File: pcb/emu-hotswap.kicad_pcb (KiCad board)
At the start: 2 copper layers, 159.1 x 114.4 mm, 74 parts, among them J1 TRRS, SW1 SW_Push, SW10 SW_Push, SW11 SW_Push, SW12 SW_Push, SW13 SW_Push, SW14 SW_Push, SW15 SW_Push, SW16 SW_Push, SW17 SW_Push, SW18 SW_Push, SW19 SW_Push, SW2 SW_Push, SW20 SW_Push, SW21 SW_Push, SW22 SW_Push, SW23 SW_Push, SW24 SW_Push, SW25 SW_Push, SW26 SW_Push, SW27 SW_Push, SW28 SW_Push, SW29 SW_Push, SW3 SW_Push, SW30 SW_Push, SW31 SW_Push, SW4 SW_Push, SW5 SW_Push, SW6 SW_Push, SW7 SW_Push, SW8 SW_Push, SW9 SW_Push, U1 ProMicro

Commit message: Work in progress
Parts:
- removed the D10 at (149.8, 127.3)
- added D10: 1N4148, used_footprints:Diode_Hybrid_SOD-123, F.Cu at (221.6, 96.2)
- added D10: 1N4148, used_footprints:Diode_Hybrid_SOD-123, F.Cu at (153.9, 131.1)
- added SW10: SW_Push, used_footprints:Switch_Mx_Hotswap_1u, F.Cu at (223.3, 91.0)
- SW10, SW15: footprint used_footprints:Switch_Mx_Hotswap_1u -> used_footprints:Switch_Mx_Hotswap_1.25u
- U1: footprint used_footprints:ProMicro_Dual -> used_footprints:Pro_Micro
- moved HM3 100.2 mm to (214.6, 75.1)
- moved HM2 59.9 mm to (134.3, 73.0)
- moved U1 26.5 mm to (112.3, 70.0), turned to 90 degrees
- moved SW30 17.5 mm to (222.7, 113.0), turned to 153 degrees
- moved D30 17.3 mm to (220.2, 117.9), turned to 153 degrees
- moved R1 11.3 mm to (225.1, 67.1)
- moved R2 11.3 mm to (222.2, 67.1)
- moved HM1 10.4 mm to (216.7, 124.0)
- moved J1 9.97 mm to (231.0, 62.3)
- moved JP1 9.97 mm to (228.9, 77.2)
- moved JP2 9.97 mm to (228.9, 77.2)
- moved JP3 9.97 mm to (233.1, 77.2)
- moved JP4 9.97 mm to (233.1, 77.2)
- moved SW25 8.29 mm to (222.7, 137.1), turned to 144 degrees
- moved D25 7.62 mm to (219.4, 141.5), turned to 144 degrees
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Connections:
- U1 pad 13: /LED -> (no net)
- U1 pad 14: Net-(U1-Pad14) -> (no net)
- U1 pad 15: Net-(U1-Pad15) -> (no net)
- U1 pad 16: Net-(U1-Pad16) -> (no net)
- U1 pad 17: Net-(U1-Pad17) -> (no net)
- U1 pad 24: Net-(U1-Pad24) -> (no net)
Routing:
- net /col4: track 367.6 -> 0.00 mm, vias 2 -> 0
- net /col5: track 361.5 -> 0.00 mm, vias 3 -> 0
- net /col3: track 341.1 -> 0.00 mm, vias 2 -> 0
- net /col2: track 301.2 -> 0.00 mm, vias 3 -> 0
- net /rowA: track 289.0 -> 0.00 mm, vias 2 -> 0
- net /rowE: track 282.7 -> 0.00 mm, vias 2 -> 0
- net /col1: track 264.9 -> 0.00 mm, vias 2 -> 0
- net GND: track 223.2 -> 0.00 mm, vias 2 -> 0
- net /rowD: track 220.0 -> 0.00 mm, vias 5 -> 0
- net /rowC: track 206.7 -> 0.00 mm, vias 7 -> 0
- net VCC: track 202.4 -> 0.00 mm, vias 1 -> 0
- net /col0: track 194.7 -> 0.00 mm, vias 2 -> 0
- net SCL: track 194.0 -> 0.00 mm, vias 2 -> 0
- net SDA: track 189.8 -> 0.00 mm, vias 8 -> 0
- net /RST: track 187.9 -> 0.00 mm, vias 1 -> 0
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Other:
- board size 159.1 x 114.4 mm -> 160.3 x 119.3 mm
- board text removed: "14.5 degrees"

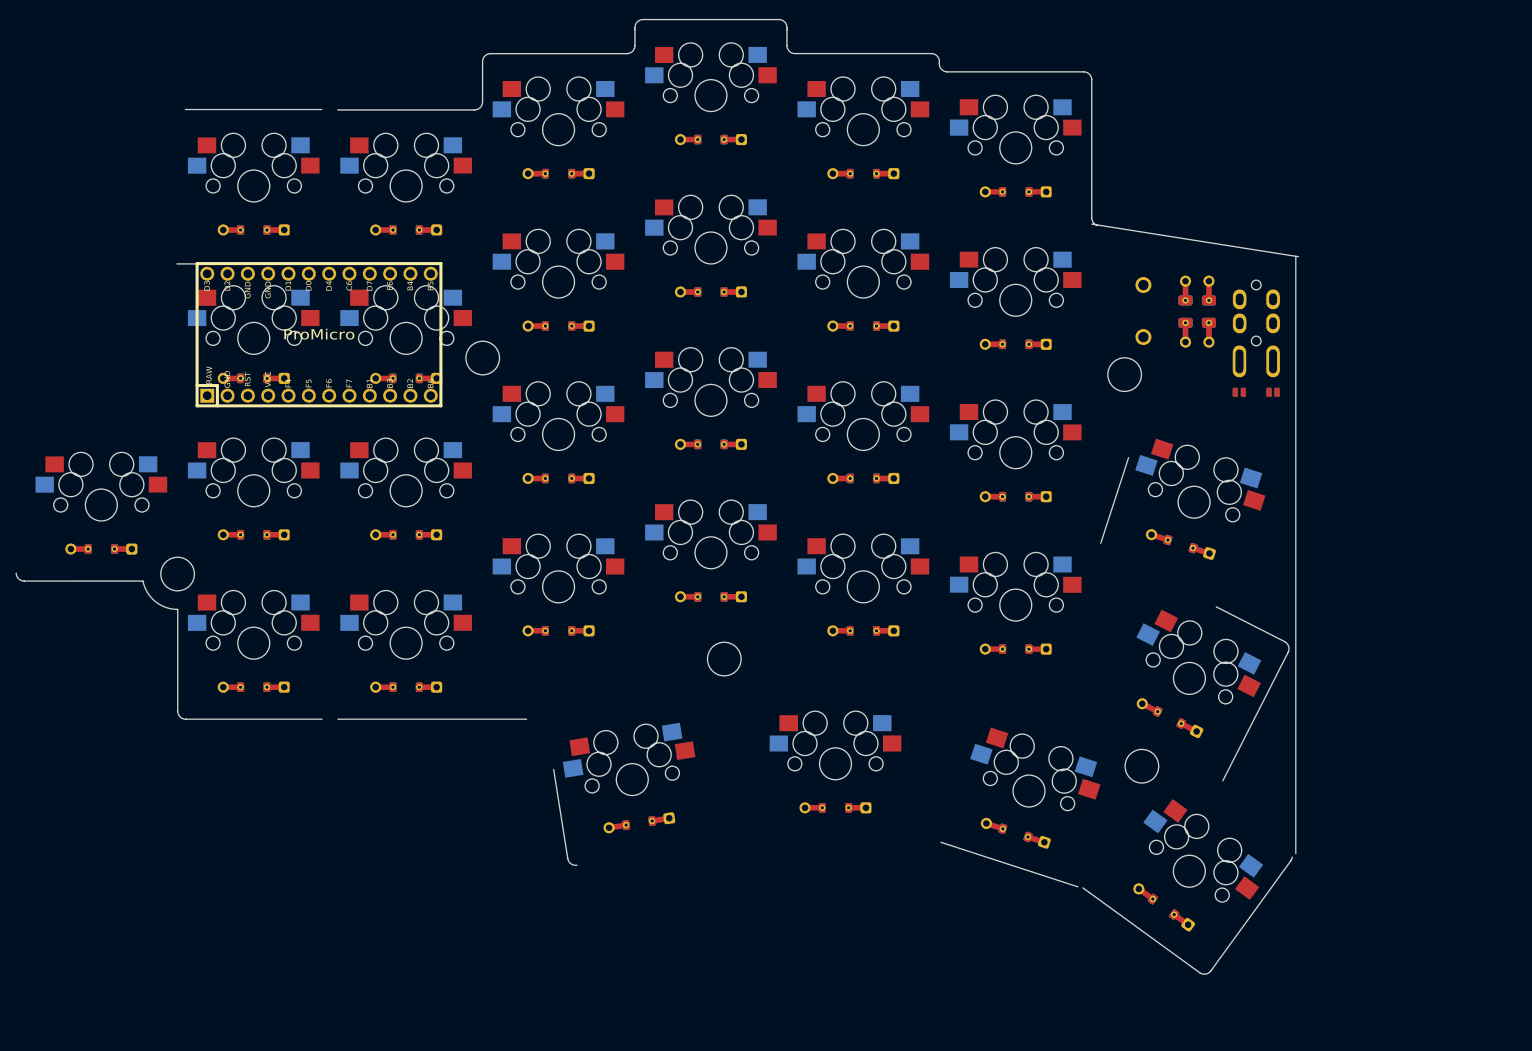
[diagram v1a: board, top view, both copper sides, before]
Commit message: Added new footprints
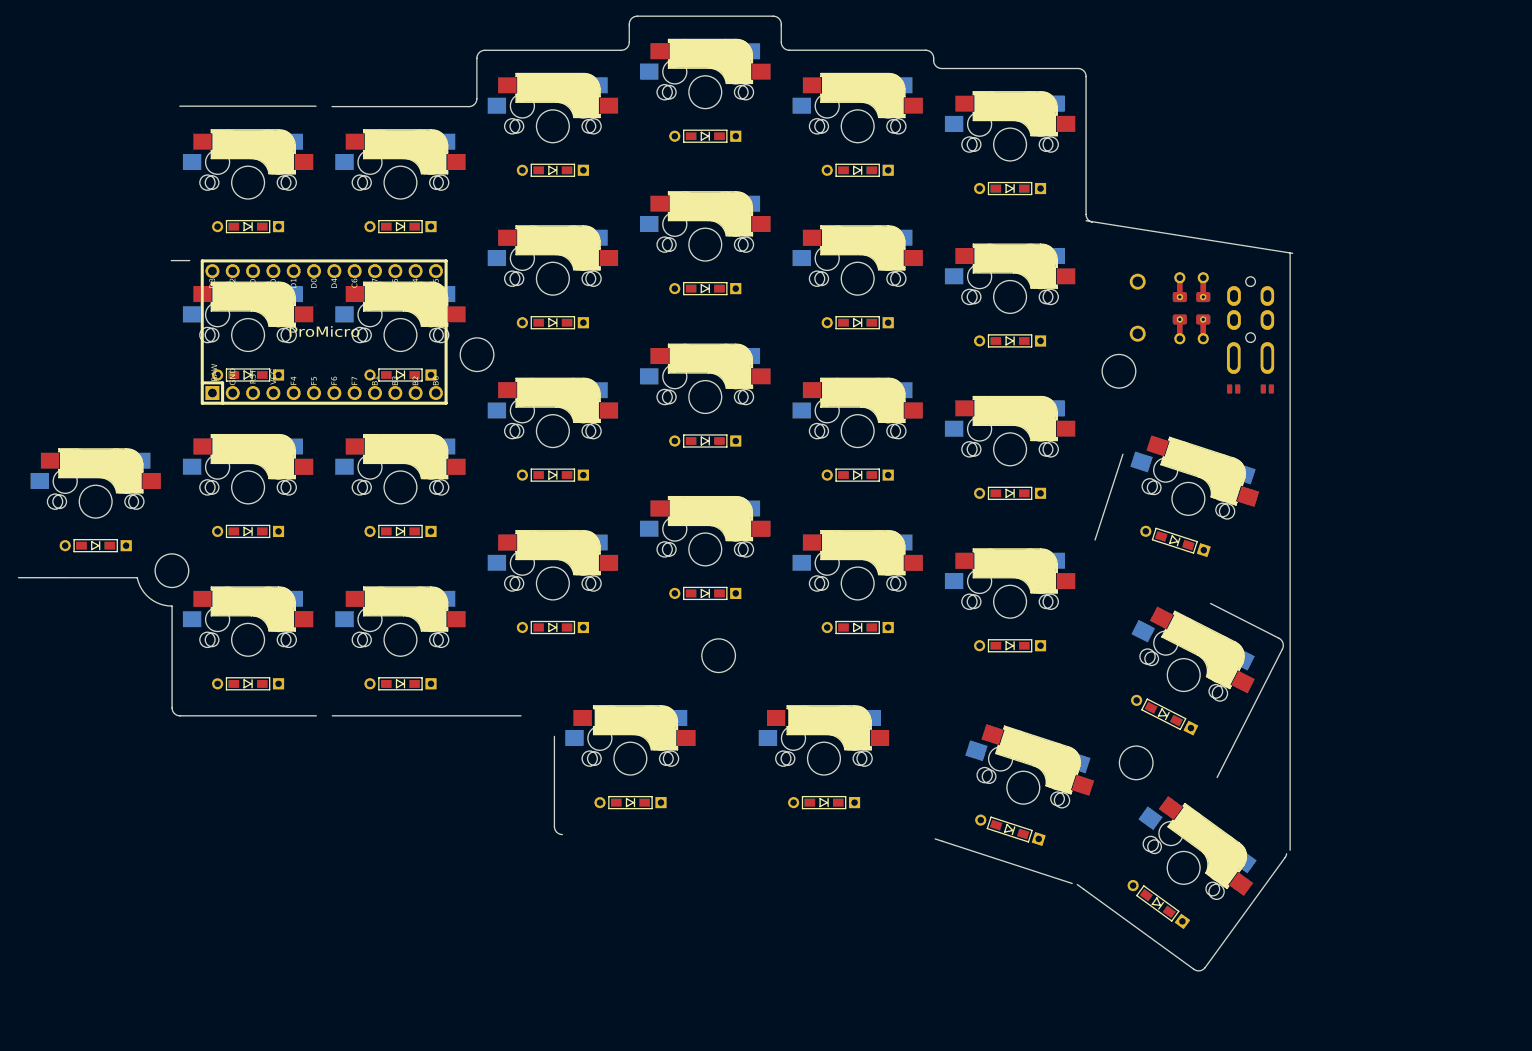
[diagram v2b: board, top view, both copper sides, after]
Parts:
- D1, D10 (x2), D11, D12, D13, D14, D15, D16, D17, D18, D19, D2, D20, D21, D22, D23, D24, D25, D26, D27, D28, D29, D3, D30, D4, D5, D6, D7, D8, D9: footprint used_footprints:Diode_Hybrid_SOD-123 -> used_footprints:D3_TH_SMD
- SW1, SW10, SW11, SW12, SW13, SW14, SW16, SW17, SW18, SW19, SW2, SW20, SW21, SW22, SW23, SW24, SW25, SW26, SW27, SW28, SW29, SW3, SW30, SW4, SW5, SW6, SW7, SW8, SW9: footprint used_footprints:Switch_Mx_Hotswap_1u -> used_footprints:CherryMX_MidHeight_Hotswap_1u
- SW10, SW15: footprint used_footprints:Switch_Mx_Hotswap_1.25u -> used_footprints:CherryMX_MidHeight_Hotswap_1.25u
- moved D10 2.77 mm to (152.8, 128.5), turned to 180 degrees
- moved SW10 2.63 mm to (152.8, 123.0), turned to 180 degrees
- moved D15 1.57 mm to (177.0, 128.5)
- moved SW15 1.57 mm to (177.0, 123.0)
- moved D10 0.82 mm to (220.8, 95.8)
- moved D11 0.82 mm to (143.1, 49.5)
- moved D12 0.82 mm to (143.1, 68.5)
- moved D13 0.82 mm to (143.1, 87.6)
- moved D14 0.82 mm to (143.1, 106.6)
- moved D17 0.82 mm to (162.2, 64.2)
- moved D18 0.82 mm to (162.2, 83.3)
- moved D19 0.82 mm to (162.2, 102.3)
- moved D21 0.82 mm to (181.2, 49.5)
- moved D22 0.82 mm to (181.2, 68.5)
- moved D23 0.82 mm to (181.2, 87.6)
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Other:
- board size 160.3 x 119.3 mm -> 159.3 x 119.3 mm

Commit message: Lined everything up to grid 0.05mm
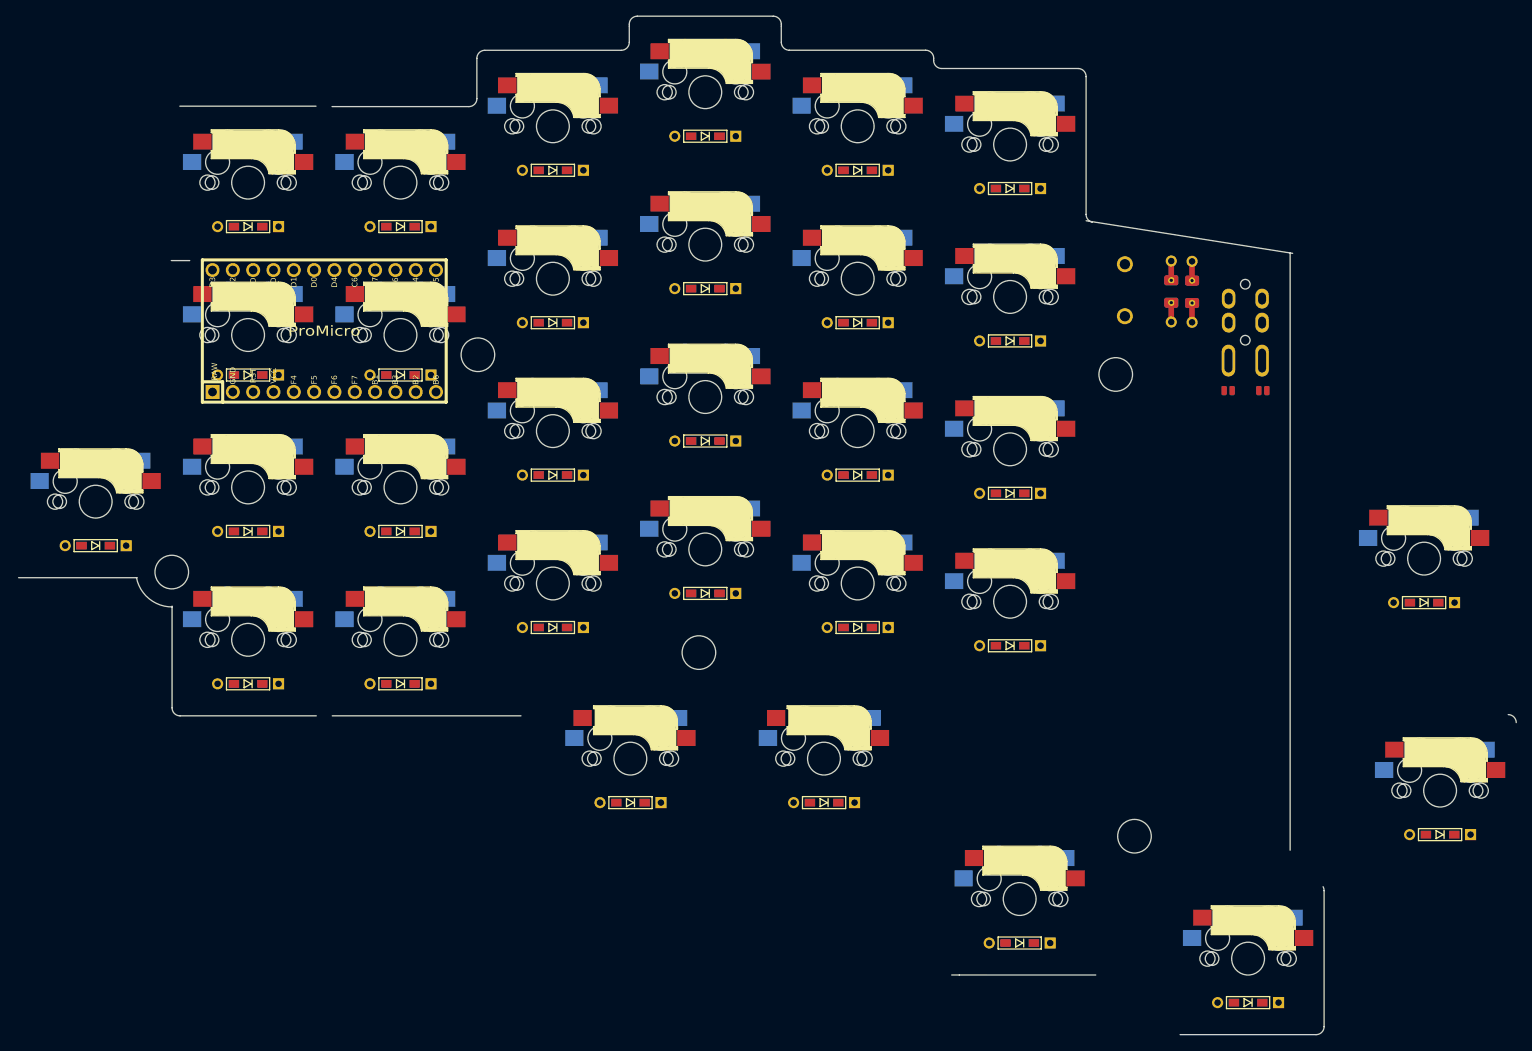
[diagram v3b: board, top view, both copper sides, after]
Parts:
- added G***: LOGO, used_footprints:emu-logo, F.Cu at (55.8, 53.5)
- moved D30 37.7 mm to (254.0, 132.5), turned to 180 degrees
- moved SW30 35.1 mm to (254.0, 127.0), turned to 180 degrees
- moved D10 32.1 mm to (252.0, 103.5), turned to 180 degrees
- moved SW10 30.4 mm to (252.0, 98.0), turned to 180 degrees
- moved D25 16.8 mm to (230.0, 153.5), turned to 180 degrees
- moved D20 14.2 mm to (201.4, 146.1), turned to 180 degrees
- moved SW20 13.9 mm to (201.4, 140.6), turned to 180 degrees
- moved SW25 13.9 mm to (230.0, 148.0), turned to 180 degrees
- moved HM1 9.17 mm to (215.8, 132.7), turned to 36 degrees
- moved SW31 2.71 mm to (214.6, 64.5)
- moved HM4 2.50 mm to (161.3, 110.5)
- moved R1 2.49 mm to (223.0, 64.7)
- moved R2 2.35 mm to (220.4, 64.6), turned to 270 degrees
- moved J1 0.74 mm to (229.7, 62.2)
- moved JP1 0.72 mm to (227.5, 77.0)
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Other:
- board size 159.3 x 119.3 mm -> 187.2 x 127.3 mm
- board text removed: "40.12"
- board text removed: "44.38"
- board text removed: "51.42"

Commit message: Positioned rows and cols
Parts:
- removed the D10 at (252.0, 103.5)
- removed the D10 at (152.8, 128.5)
- removed the SW10 at (152.8, 123.0)
- removed the SW10 at (252.0, 98.0)
- added D10: 1N4148, used_footprints:D3_TH_SMD, F.Cu at (220.4, 95.8)
- added D10: 1N4148, used_footprints:D3_TH_SMD, F.Cu at (153.3, 130.1)
- added SW10: SW_Push, used_footprints:CherryMX_MidHeight_Hotswap_1.25u, F.Cu at (152.5, 124.6)
- added SW10: SW_Push, used_footprints:CherryMX_MidHeight_Hotswap_1u, F.Cu at (222.1, 90.6)
- moved HM1 40.5 mm to (253.8, 146.6)
- moved D30 38.4 mm to (218.7, 117.3), turned to 153 degrees
- moved SW30 35.9 mm to (221.2, 112.4), turned to 153 degrees
- moved D25 17.6 mm to (218.1, 140.5), turned to 144 degrees
- moved D20 14.8 mm to (200.1, 131.3), turned to 162 degrees
- moved SW25 14.7 mm to (221.4, 136.1), turned to 144 degrees
- moved SW20 14.5 mm to (201.8, 126.1), turned to 162 degrees
- moved D15 0.83 mm to (177.8, 128.2)
- moved SW15 0.83 mm to (177.8, 122.7)
- moved D5 0.50 mm to (85.9, 96.9)
- moved SW5 0.50 mm to (85.9, 91.4)
- moved D16 0.25 mm to (162.2, 45.5)
- moved D17 0.25 mm to (162.2, 64.5)
- moved D18 0.25 mm to (162.2, 83.5)
- moved D19 0.25 mm to (162.2, 102.6)
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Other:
- board size 187.2 x 127.3 mm -> 160.1 x 118.5 mm
- board text removed: "46.66"

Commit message: Roughly cut edges, fixed footprints on the scheme.
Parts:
- removed the D10 at (220.4, 95.8)
- removed the D10 at (153.3, 130.1)
- removed G***: LOGO, used_footprints:emu-logo
- removed the SW10 at (152.5, 124.6)
- removed the SW10 at (222.1, 90.6)
- added D10: 1N4148, used_footprints:Diode_Hybrid_SOD-123, F.Cu at (153.3, 130.1)
- added D31: 1N4148, used_footprints:Diode_Hybrid_SOD-123, F.Cu at (220.4, 95.8)
- added SW10: SW_Push, used_footprints:Switch_Mx_Hotswap_1u, F.Cu at (152.5, 124.6)
- added SW31: SW_Push, used_footprints:Switch_Mx_Hotswap_1u, F.Cu at (222.1, 90.6)
- D1, D11, D12, D13, D14, D15, D16, D17, D18, D19, D2, D20, D21, D22, D23, D24, D25, D26, D27, D28, D29, D3, D30, D4, D5, D6, D7, D8, D9: footprint used_footprints:D3_TH_SMD -> used_footprints:Diode_Hybrid_SOD-123
- SW1, SW11, SW12, SW13, SW14, SW16, SW17, SW18, SW19, SW2, SW20, SW21, SW22, SW23, SW24, SW25, SW26, SW27, SW28, SW29, SW3, SW30, SW4, SW5, SW6, SW7, SW8, SW9: footprint used_footprints:CherryMX_MidHeight_Hotswap_1u -> used_footprints:Switch_Mx_Hotswap_1u
- SW15: footprint used_footprints:CherryMX_MidHeight_Hotswap_1.25u -> used_footprints:Switch_Mx_Hotswap_1u
- U1: footprint used_footprints:Pro_Micro -> used_footprints:ArduinoProMicro
- moved HM1 44.8 mm to (215.5, 123.3)
- moved D7 19.6 mm to (143.1, 70.6)
- moved D2 8.31 mm to (96.8, 74.0), turned to 90 degrees
- moved U1 0.95 mm to (114.0, 69.5), turned to 0 degrees
- renumbered SW31 to SW32
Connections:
- U1 pad 17: (no net) -> /rowF
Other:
- board size 160.1 x 118.5 mm -> 157.8 x 118.3 mm
